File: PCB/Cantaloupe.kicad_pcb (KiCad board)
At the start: 2 copper layers, 149.9 x 122.2 mm, 117 parts, among them J1 RGB_Out, J2 SWD, J3 Trackpad, J4 OLED, J5 Extra, J6 USB_In, J7 Split_comm_link, Q1 AO6802, SW1 MX, SW10 MX, SW11 MX, SW12 MX, SW13 MX, SW14 MX, SW15 MX, SW16 MX, SW17 MX, SW18 MX, SW19 MX, SW2 MX, SW20 MX, SW21 MX, SW22 MX, SW23 MX, SW24 MX, SW25 MX, SW26 MX, SW27 MX, SW28 MX, SW29 MX, SW3 MX, SW30 MX, SW31 Encoder, SW32 Reset, SW4 MX, SW5 MX, SW6 MX, SW7 MX, SW8 MX, SW9 MX, U1 STM32F401CCU6, U2 MB85RS64, U3 SRV05-4, U4 SRV05-4, U5 W25Q128JVS, U6 XC6206P332MR, Y1 8MHz

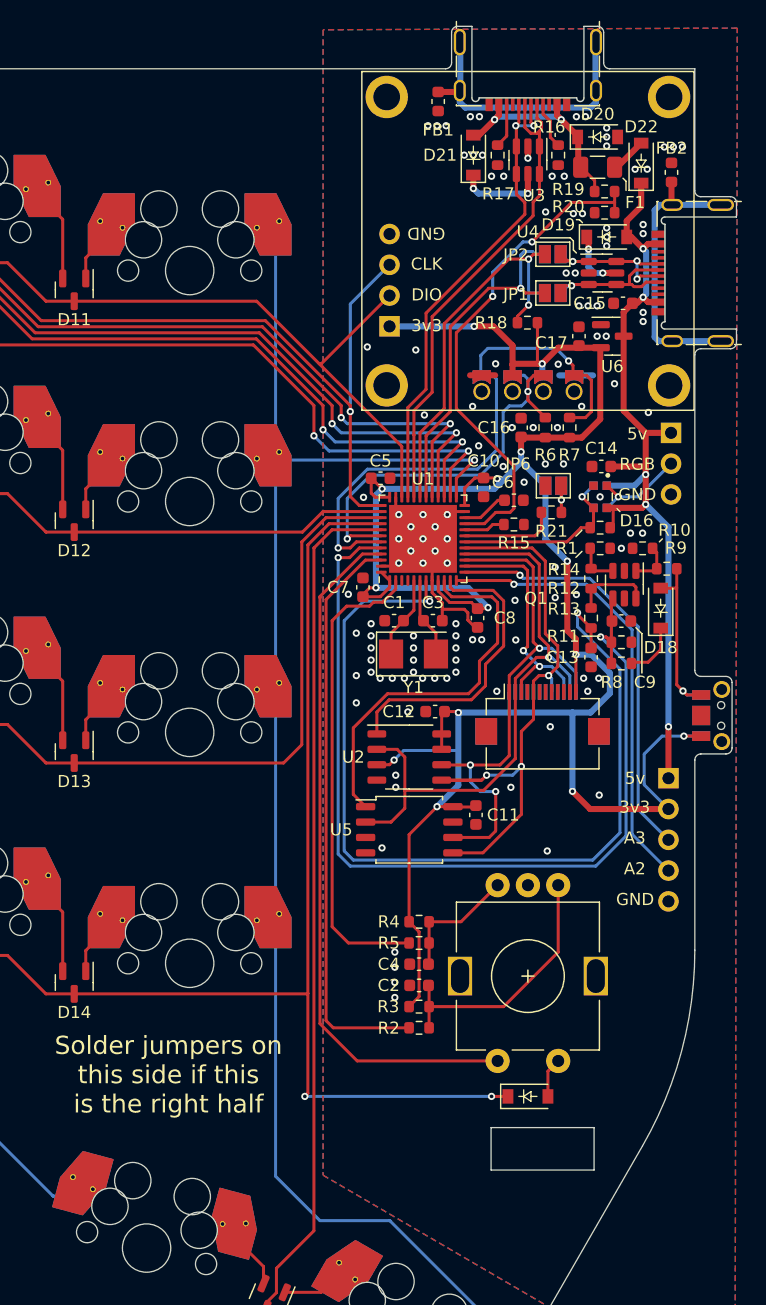
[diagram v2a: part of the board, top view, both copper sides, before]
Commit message: 30/5/2022 changes
Changed XC6206P332MR-G to XC6220B331MR-G for more power output. Changed fuse to 1A. Fixed library links. Changed AO6802 back to two AO3400s. Moved reset circuit downwards and extra pin header upwards for better routing. Updated BOM.
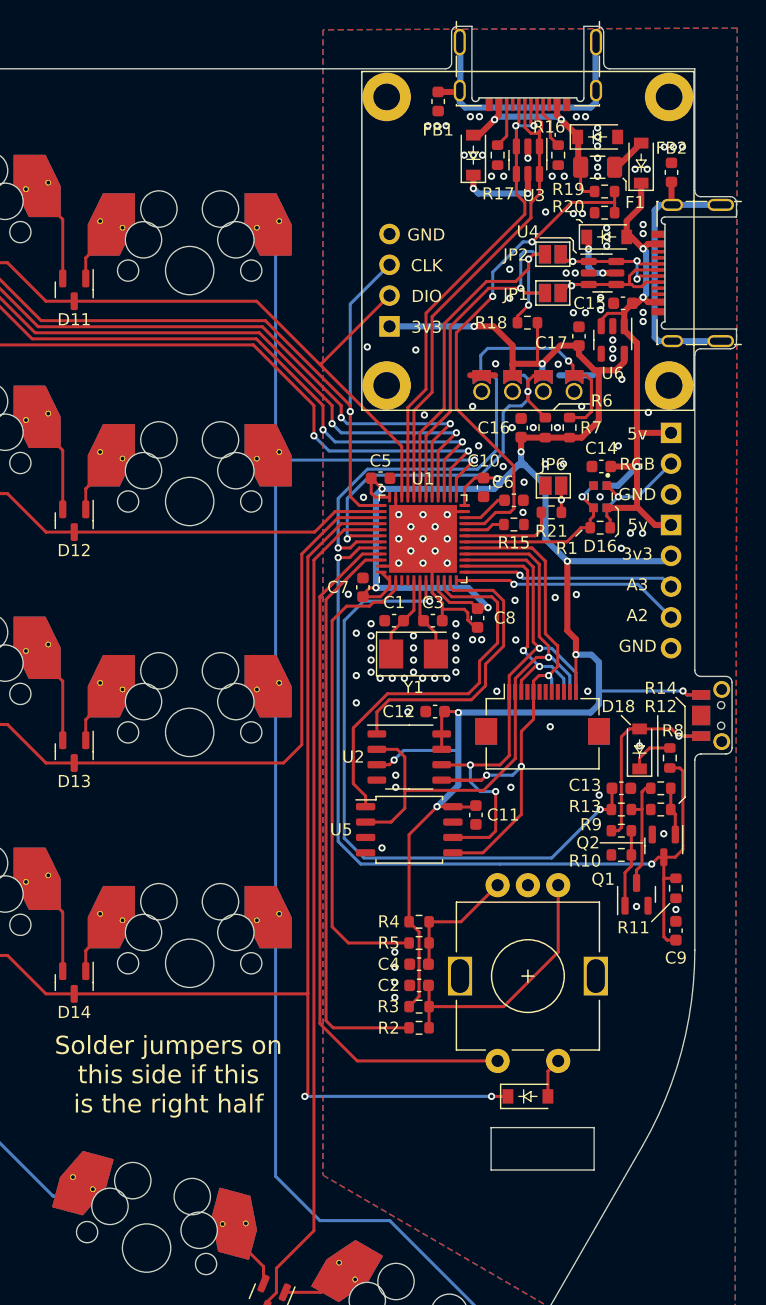
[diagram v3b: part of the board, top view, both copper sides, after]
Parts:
- added Q2: AO3400A, Package_TO_SOT_SMD:SOT-23, F.Cu at (201.3, 116.2)
- A1: footprint Ariamelon:Ariamelon_Logo_x3_CU -> Cantaloupe:Ariamelon_Logo_x3_CU
- D16: footprint Ariamelon:LED_WS2812-2020_Flippable -> Cantaloupe:LED_WS2812-2020_Flippable
- D17, D18, D20: footprint Ariamelon:D_SOD-123 -> Cantaloupe:D_SOD-123
- D19, D21, D22: value B5819W-TP -> B5819W SL; footprint Ariamelon:D_SOD-123 -> Cantaloupe:D_SOD-123
- F1: value nSMD050 -> nSMD100
- J1: footprint Ariamelon:PinHeader_1x03_P2.54mm_Vertical_Silkless -> Cantaloupe:PinHeader_1x03_P2.54mm_Vertical_Silkless
- J2: footprint Ariamelon:PinHeader_1x04_P2.54mm_Vertical_SIlkless -> Cantaloupe:PinHeader_1x04_P2.54mm_Vertical_SIlkless
- J3: footprint Ariamelon:Hirose_FH12-12S-0.5SH_1x12-1MP_P0.50mm_Horizontal_Flippable -> Cantaloupe:Hirose_FH12-12S-0.5SH_1x12-1MP_P0.50mm_Horizontal_Flippable
- J4: footprint Ariamelon:OLED_0.96_SSD1306_128x64_Flippable_Reversepads -> Cantaloupe:OLED_0.96_SSD1306_128x64_Flippable_Reversepads
- J5: footprint Ariamelon:PinHeader_1x05_P2.54mm_Vertical_Silkless -> Cantaloupe:PinHeader_1x05_P2.54mm_Vertical_Silkless
- J6, J7: footprint Ariamelon:HRO-TYPE-C-31-M-13x -> Cantaloupe:HRO-TYPE-C-31-M-13x
- Q1: value AO6802 -> AO3400A; footprint Package_TO_SOT_SMD:SOT-23-6 -> Package_TO_SOT_SMD:SOT-23
- R19: value 100k -> 5.1k
- R20: value 200k -> 10k
- R6, R7: value 4.7k -> 4k7
- SW1, SW10, SW11, SW12, SW13, SW14, SW15, SW16, SW17, SW18, SW19, SW2, SW20, SW21, SW22, SW23, SW24, SW25, SW26, SW27, SW28, SW29, SW3, SW30, SW4, SW5, SW6, SW7, SW8, SW9: footprint Ariamelon:MXOnly-1U-Hotswap-Dual -> Cantaloupe:MXOnly-1U-Hotswap-Dual
- SW31: footprint Ariamelon:EC11_Flippable -> Cantaloupe:EC11_Flippable
- SW32: footprint Ariamelon:Switch_TS24ZJ_Flippable -> Cantaloupe:Switch_TS24ZJ_Flippable
- U6: value XC6206P332MR -> XC6220B331MR-G; footprint Package_TO_SOT_SMD:SOT-23 -> Package_TO_SOT_SMD:SOT-23-5
- moved C9 25.9 mm to (202.3, 123.2), turned to 90 degrees
- moved Q1 25.6 mm to (199.1, 120.2), turned to 90 degrees
- moved R10 25.4 mm to (197.8, 116.9)
- moved R14 22.1 mm to (201.1, 113.2), turned to 180 degrees
- moved R9 21.9 mm to (197.8, 114.9), turned to 0 degrees
- moved J5 20.9 mm to (201.9, 89.7)
- moved R11 20.8 mm to (202.3, 119.7), turned to -90 degrees
- moved R12 18.2 mm to (201.1, 111.4), turned to 180 degrees
- moved R13 16.0 mm to (197.8, 113.2), turned to 180 degrees
- moved D18 11.7 mm to (199.3, 108.2)
- moved C13 11.1 mm to (197.8, 111.4), turned to 180 degrees
- moved R8 8.77 mm to (201.8, 108.9), turned to 90 degrees
- moved U6 0.32 mm to (197.1, 74.5), turned to -90 degrees
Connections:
- Q1 pad 3: Net-(Q1-Pad3) -> Net-(R12-Pad2)
- R12 pad 1: Net-(Q1-Pad3) -> Net-(R12-Pad1)
- R12 pad 2: Net-(Q1-Pad6) -> Net-(R12-Pad2)
- R13 pad 1: Net-(Q1-Pad6) -> Net-(R12-Pad2)
- R14 pad 1: Net-(Q1-Pad3) -> Net-(R12-Pad1)
- SW32 pad 1: Net-(D18-Pad2) -> +3V3
- SW32 pad 2: +3V3 -> Net-(D18-Pad2)
- U6 pad 1: GND -> +5V
- U6 pad 2: +3V3 -> GND
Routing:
- net NRST: track 75.5 -> 53.6 mm
- net +5V: track 69.8 -> 50.7 mm, vias 5 -> 3
- net A2: track 37.3 -> 19.0 mm
- net A3: track 34.8 -> 17.5 mm
- net Net-(R12-Pad2): track 0.00 -> 9.44 mm
- net Net-(Q1-Pad6): track 6.45 -> 0.00 mm
- net +3V3: track 200.7 -> 194.8 mm, vias 14 -> 13
- net Net-(R12-Pad1): track 0.00 -> 3.97 mm
- net BOOT0: track 77.1 -> 73.4 mm
- net Net-(Q1-Pad3): track 3.21 -> 0.00 mm
- net Net-(D18-Pad2): track 14.9 -> 18.0 mm
- net Net-(R10-Pad2): track 3.37 -> 6.40 mm
- net Link-: track 12.1 -> 13.0 mm
- net Net-(D18-Pad1): track 4.52 -> 3.74 mm
- net ROW3: track 168.9 -> 168.3 mm
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
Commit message: Better routing
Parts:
- FB1, FB2: value BLM18KG260 -> GZ1608D110TF
- SW1, SW10, SW11, SW12, SW13, SW14, SW15, SW16, SW17, SW18, SW19, SW2, SW20, SW21, SW22, SW23, SW24, SW25, SW26, SW27, SW28, SW29, SW3, SW30, SW4, SW5, SW6, SW7, SW8, SW9: footprint Cantaloupe:MXOnly-1U-Hotswap-Dual -> Cantaloupe:MX_Choc-1U-Hotswap-Dual
- U1: value STM32F401CCU6 -> STM32F411CCU6
- moved D1 5.50 mm to (79.0, 79.2)
- moved D2 5.50 mm to (79.0, 98.2)
- moved D4 5.50 mm to (79.0, 136.3)
- moved D5 5.50 mm to (79.0, 155.4)
- moved D3 5.50 mm to (79.0, 117.3)
- moved D11 3.91 mm to (152.7, 74.2)
- moved D12 3.91 mm to (152.7, 93.3)
- moved D14 3.91 mm to (152.7, 131.4)
- moved D13 3.91 mm to (152.7, 112.3)
- moved D6 3.65 mm to (117.2, 69.7)
- moved D7 3.65 mm to (117.2, 88.7)
- moved D8 3.65 mm to (117.2, 107.8)
- moved D10 3.65 mm to (117.2, 145.9)
- moved D9 3.65 mm to (117.2, 126.8)
- moved A1 1.59 mm to (128.7, 131.9)
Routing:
- net COL0: track 231.8 -> 308.9 mm
- net COL2: track 183.3 -> 257.7 mm
- net COL5: track 119.9 -> 181.7 mm
- net COL4: track 154.5 -> 215.5 mm
- net COL1: track 193.7 -> 248.1 mm
- net COL3: track 158.0 -> 210.3 mm
- net Net-(D2-Pad2): track 3.81 -> 23.0 mm
- net Net-(D1-Pad2): track 3.81 -> 23.0 mm
- net Net-(D3-Pad2): track 3.81 -> 23.0 mm
- net Net-(D4-Pad2): track 3.81 -> 23.0 mm
- net Net-(D5-Pad2): track 3.81 -> 23.0 mm
- net Net-(D9-Pad2): track 3.81 -> 22.1 mm
- net Net-(D6-Pad2): track 3.81 -> 22.1 mm
- net Net-(D8-Pad2): track 3.81 -> 22.1 mm
- net Net-(D7-Pad2): track 3.81 -> 22.1 mm
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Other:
- board text added: "Cantaloupe V2.2"
- board text removed: "Cantaloupe V2.1"

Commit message: INCOMPLETE V3.0 Initial Update
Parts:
- removed J7: Split_comm_link, Cantaloupe:HRO-TYPE-C-31-M-13x
- removed JP4: Link+_L, Jumper:SolderJumper-2_P1.3mm_Open_Pad1.0x1.5mm
- removed JP5: Side_L, Jumper:SolderJumper-2_P1.3mm_Open_Pad1.0x1.5mm
- removed JP6: Side_R, Jumper:SolderJumper-2_P1.3mm_Open_Pad1.0x1.5mm
- removed Q2: AO3400A, Package_TO_SOT_SMD:SOT-23
- removed R21: 10k, Resistor_SMD:R_0603_1608Metric
- added C18: 100n, Capacitor_SMD:C_0402_1005Metric, B.Cu at (138.6, 57.1)
- added C19: 4u7, Capacitor_SMD:C_0603_1608Metric, B.Cu at (153.7, 103.9)
- added C20: 100n, Capacitor_SMD:C_0402_1005Metric, B.Cu at (153.7, 106.4)
- added C21: 100n, Capacitor_SMD:C_0402_1005Metric, B.Cu at (144.6, 46.2)
- added C22: 100n, Capacitor_SMD:C_0402_1005Metric, B.Cu at (147.4, 50.5)
- added C23: 100n, Capacitor_SMD:C_0402_1005Metric, B.Cu at (132.7, 50.5)
- added C24: 1u, Capacitor_SMD:C_0603_1608Metric, B.Cu at (153.8, 90.0)
- added C25: 100n, Cantaloupe:C_0402_1005Metric, B.Cu at (16.6, 55.4)
- added C26: 100n, Cantaloupe:C_0402_1005Metric, B.Cu at (26.2, 75.9)
- added C27: 100n, Cantaloupe:C_0402_1005Metric, B.Cu at (16.6, 93.5)
- added C28: 100n, Cantaloupe:C_0402_1005Metric, B.Cu at (26.2, 114.0)
- added C29: 100n, Cantaloupe:C_0402_1005Metric, B.Cu at (16.6, 131.6)
- added C30: 100n, Cantaloupe:C_0402_1005Metric, B.Cu at (35.6, 53.0)
- added C31: 100n, Cantaloupe:C_0402_1005Metric, B.Cu at (45.2, 73.5)
- added C32: 100n, Cantaloupe:C_0402_1005Metric, B.Cu at (35.6, 91.1)
- added C33: 100n, Cantaloupe:C_0402_1005Metric, B.Cu at (45.2, 111.6)
- added C34: 100n, Cantaloupe:C_0402_1005Metric, B.Cu at (35.6, 129.2)
- added C35: 100n, Cantaloupe:C_0402_1005Metric, B.Cu at (54.7, 48.3)
- added C36: 100n, Cantaloupe:C_0402_1005Metric, B.Cu at (64.3, 68.8)
- added C37: 100n, Cantaloupe:C_0402_1005Metric, B.Cu at (54.7, 86.4)
- added C38: 100n, Cantaloupe:C_0402_1005Metric, B.Cu at (64.3, 106.9)
- added C39: 100n, Cantaloupe:C_0402_1005Metric, B.Cu at (54.7, 124.5)
- added C40: 100n, Cantaloupe:C_0402_1005Metric, B.Cu at (73.7, 44.3)
- added C41: 100n, Cantaloupe:C_0402_1005Metric, B.Cu at (83.3, 64.8)
- added C42: 100n, Cantaloupe:C_0402_1005Metric, B.Cu at (73.7, 82.4)
- added C43: 100n, Cantaloupe:C_0402_1005Metric, B.Cu at (83.3, 102.9)
- added C44: 100n, Cantaloupe:C_0402_1005Metric, B.Cu at (86.4, 129.2)
- added C45: 100n, Cantaloupe:C_0402_1005Metric, B.Cu at (92.8, 48.3)
- added C46: 100n, Cantaloupe:C_0402_1005Metric, B.Cu at (102.4, 68.8)
- added C47: 100n, Cantaloupe:C_0402_1005Metric, B.Cu at (92.8, 86.4)
- added C48: 100n, Cantaloupe:C_0402_1005Metric, B.Cu at (102.4, 106.9)
- added C49: 100n, Cantaloupe:C_0402_1005Metric, B.Cu at (107.4, 130.7)
- added C50: 100n, Cantaloupe:C_0402_1005Metric, B.Cu at (111.8, 51.5)
- added C51: 100n, Cantaloupe:C_0402_1005Metric, B.Cu at (121.4, 72.0)
- added C52: 100n, Cantaloupe:C_0402_1005Metric, B.Cu at (111.8, 89.6)
- added C53: 100n, Cantaloupe:C_0402_1005Metric, B.Cu at (121.4, 110.1)
- added C54: 100n, Cantaloupe:C_0402_1005Metric, B.Cu at (127.1, 137.6)
- added D23: 1N4148, Cantaloupe:D_SOD-323, B.Cu at (88.4, 75.6)
- added D24: 1N4148, Cantaloupe:D_SOD-323, B.Cu at (88.4, 94.6)
- added D25: 1N4148, Cantaloupe:D_SOD-323, B.Cu at (105.9, 119.1)
- added D26: 1N4148, Cantaloupe:D_SOD-323, B.Cu at (107.4, 40.7)
- added D27: 1N4148, Cantaloupe:D_SOD-323, B.Cu at (107.4, 59.7)
- added D28: 1N4148, Cantaloupe:D_SOD-323, B.Cu at (107.4, 78.8)
- added D29: 1N4148, Cantaloupe:D_SOD-323, B.Cu at (107.4, 97.8)
- added D30: 1N4148, Cantaloupe:D_SOD-323, B.Cu at (128.7, 126.0)
- added D31: SK6812MINI-E, Cantaloupe:YS-SK6812MINI-E-Flippable, B.Cu at (21.4, 56.1)
- added D32: SK6812MINI-E, Cantaloupe:YS-SK6812MINI-E-Flippable, B.Cu at (21.4, 75.2)
- added D33: SK6812MINI-E, Cantaloupe:YS-SK6812MINI-E-Flippable, B.Cu at (21.4, 94.2)
- added D34: SK6812MINI-E, Cantaloupe:YS-SK6812MINI-E-Flippable, B.Cu at (21.4, 113.3)
- added D35: SK6812MINI-E, Cantaloupe:YS-SK6812MINI-E-Flippable, B.Cu at (21.4, 132.3)
- added D36: SK6812MINI-E, Cantaloupe:YS-SK6812MINI-E-Flippable, B.Cu at (40.4, 53.8)
- added D37: SK6812MINI-E, Cantaloupe:YS-SK6812MINI-E-Flippable, B.Cu at (40.4, 72.8)
- added D38: SK6812MINI-E, Cantaloupe:YS-SK6812MINI-E-Flippable, B.Cu at (40.4, 91.9)
- added D39: SK6812MINI-E, Cantaloupe:YS-SK6812MINI-E-Flippable, B.Cu at (40.4, 110.9)
- added D40: SK6812MINI-E, Cantaloupe:YS-SK6812MINI-E-Flippable, B.Cu at (40.4, 130.0)
- added D41: SK6812MINI-E, Cantaloupe:YS-SK6812MINI-E-Flippable, B.Cu at (59.5, 49.0)
- added D42: SK6812MINI-E, Cantaloupe:YS-SK6812MINI-E-Flippable, B.Cu at (59.5, 68.1)
- added D43: SK6812MINI-E, Cantaloupe:YS-SK6812MINI-E-Flippable, B.Cu at (59.5, 87.1)
- added D44: SK6812MINI-E, Cantaloupe:YS-SK6812MINI-E-Flippable, B.Cu at (59.5, 106.2)
- added D45: SK6812MINI-E, Cantaloupe:YS-SK6812MINI-E-Flippable, B.Cu at (59.5, 125.2)
- added D46: SK6812MINI-E, Cantaloupe:YS-SK6812MINI-E-Flippable, B.Cu at (78.5, 45.0)
- added D47: SK6812MINI-E, Cantaloupe:YS-SK6812MINI-E-Flippable, B.Cu at (78.5, 64.1)
- added D48: SK6812MINI-E, Cantaloupe:YS-SK6812MINI-E-Flippable, B.Cu at (78.5, 83.1)
- added D49: SK6812MINI-E, Cantaloupe:YS-SK6812MINI-E-Flippable, B.Cu at (78.5, 102.2)
- added D50: SK6812MINI-E, Cantaloupe:YS-SK6812MINI-E-Flippable, B.Cu at (91.2, 130.0)
- added D51: SK6812MINI-E, Cantaloupe:YS-SK6812MINI-E-Flippable, B.Cu at (97.6, 49.0)
- added D52: SK6812MINI-E, Cantaloupe:YS-SK6812MINI-E-Flippable, B.Cu at (97.6, 68.1)
- added D53: SK6812MINI-E, Cantaloupe:YS-SK6812MINI-E-Flippable, B.Cu at (97.6, 87.1)
- added D54: SK6812MINI-E, Cantaloupe:YS-SK6812MINI-E-Flippable, B.Cu at (97.6, 106.2)
- added D55: SK6812MINI-E, Cantaloupe:YS-SK6812MINI-E-Flippable, B.Cu at (111.8, 132.7)
- added D56: SK6812MINI-E, Cantaloupe:YS-SK6812MINI-E-Flippable, B.Cu at (116.6, 52.2)
- added D57: SK6812MINI-E, Cantaloupe:YS-SK6812MINI-E-Flippable, B.Cu at (116.6, 71.2)
- added D58: SK6812MINI-E, Cantaloupe:YS-SK6812MINI-E-Flippable, B.Cu at (116.6, 90.3)
- added D59: SK6812MINI-E, Cantaloupe:YS-SK6812MINI-E-Flippable, B.Cu at (116.6, 109.3)
- added D60: SK6812MINI-E, Cantaloupe:YS-SK6812MINI-E-Flippable, B.Cu at (130.9, 140.6)
- added D67: B5819W SL, Cantaloupe:D_SOD-123, B.Cu at (141.3, 35.7)
- added D68: SMF5.0A, Cantaloupe:D_SOD-123, B.Cu at (116.1, 34.6)
- added D69: B5819W SL, Cantaloupe:D_SOD-123, B.Cu at (116.1, 37.1)
- added D70: B5819W SL, Cantaloupe:D_SOD-123, B.Cu at (125.7, 37.1)
- added H1: Tooling Hole, Cantaloupe:JLC Tooling Hole, F.Cu at (156.8, 30.3)
- added H2: Tooling Hole, Cantaloupe:JLC Tooling Hole, F.Cu at (11.2, 41.7)
- added H3: Tooling Hole, Cantaloupe:JLC Tooling Hole, F.Cu at (137.0, 150.1)
- added SW33: Reset, Cantaloupe:SW_SPST_TL3342-Dual, F.Cu at (154.7, 63.3)
- added U7: AP2127K-ADJ, Package_TO_SOT_SMD:SOT-23-5, B.Cu at (155.3, 86.3)
- A1, F1, Q1, U4: moved to B.Cu
- C1: value 20p -> 10n; footprint Capacitor_SMD:C_0603_1608Metric -> Capacitor_SMD:C_0402_1005Metric; moved to B.Cu
- C10, C13, C14: footprint Capacitor_SMD:C_0603_1608Metric -> Capacitor_SMD:C_0402_1005Metric; moved to B.Cu
- C11, C12, C5: value 100n -> 1u; moved to B.Cu
- C15, C16, C17, C9: value 10u -> 100n; footprint Capacitor_SMD:C_0603_1608Metric -> Capacitor_SMD:C_0402_1005Metric; moved to B.Cu
- C2: value 100n -> 10n; footprint Capacitor_SMD:C_0603_1608Metric -> Capacitor_SMD:C_0402_1005Metric; moved to B.Cu
- C3: value 20p -> 4u7; moved to B.Cu
- C4: value 100n -> 4u7; moved to B.Cu
- C6: value 4.7u -> 100n; footprint Capacitor_SMD:C_0603_1608Metric -> Capacitor_SMD:C_0402_1005Metric; moved to B.Cu
- C7, C8: value 100n -> 22p; footprint Capacitor_SMD:C_0603_1608Metric -> Capacitor_SMD:C_0402_1005Metric; moved to B.Cu
- D1, D10, D11, D12, D13, D14, D15, D2, D3, D4, D5, D6, D7, D8, D9: value D_Dual_CommonCathode_AAK_Split_Small -> 1N4148; footprint Package_TO_SOT_SMD:SOT-23 -> Cantaloupe:D_SOD-323; moved to B.Cu
- D16: value WS2812C-2020 -> 1N4148; footprint Cantaloupe:LED_WS2812-2020_Flippable -> Cantaloupe:D_SOD-323; moved to B.Cu
- D17, D18: value D -> 1N4148; footprint Cantaloupe:D_SOD-123 -> Cantaloupe:D_SOD-323; moved to B.Cu
- D19, D21, D22: value B5819W SL -> 1N4148; footprint Cantaloupe:D_SOD-123 -> Cantaloupe:D_SOD-323; moved to B.Cu
- D20: value SMF5.0A -> 1N4148; footprint Cantaloupe:D_SOD-123 -> Cantaloupe:D_SOD-323; moved to B.Cu
- FB1, FB2: value GZ1608D110TF -> 60R@100MHz; footprint Inductor_SMD:L_0603_1608Metric -> Inductor_SMD:L_1206_3216Metric; moved to B.Cu
- J1: value RGB_Out -> SWD; footprint Cantaloupe:PinHeader_1x03_P2.54mm_Vertical_Silkless -> Connector_PinHeader_2.54mm:PinHeader_1x04_P2.54mm_Vertical
- J2: value SWD -> USB_In; footprint Cantaloupe:PinHeader_1x04_P2.54mm_Vertical_SIlkless -> Cantaloupe:HRO-TYPE-C-31-M-13x
- J3: value Trackpad -> Split_comm_link; footprint Cantaloupe:Hirose_FH12-12S-0.5SH_1x12-1MP_P0.50mm_Horizontal_Flippable -> Cantaloupe:HRO-TYPE-C-31-M-13x; moved to B.Cu
- J4: value OLED -> Trackpad; footprint Cantaloupe:OLED_0.96_SSD1306_128x64_Flippable_Reversepads -> Cantaloupe:Hirose_FH12-12S-0.5SH_1x12-1MP_P0.50mm_Horizontal_Flippable; moved to B.Cu
- J5: value Extra -> OLED; footprint Cantaloupe:PinHeader_1x05_P2.54mm_Vertical_Silkless -> Cantaloupe:OLED_1.5_SSD1315_128x128_NoPins
- J6: value USB_In -> OLED_PH; footprint Cantaloupe:HRO-TYPE-C-31-M-13x -> Cantaloupe:JST_PH_S7B-PH-K_1x07_P2.00mm_Horizontal-Dual
- JP1: value Link-_R -> Side_L; moved to B.Cu
- JP2: value Link+_R -> Side_R; moved to B.Cu
- JP3: value Link-_L -> MISO_Pullup
- R1, R16, R17: value 5k1 -> 10k; footprint Resistor_SMD:R_0603_1608Metric -> Resistor_SMD:R_0402_1005Metric; moved to B.Cu
- R10: value 10k -> 1k; footprint Resistor_SMD:R_0603_1608Metric -> Resistor_SMD:R_0402_1005Metric; moved to B.Cu
- R11: value 1M -> 5k1; footprint Resistor_SMD:R_0603_1608Metric -> Resistor_SMD:R_0402_1005Metric; moved to B.Cu
- R12: value 10k -> 5k1; footprint Resistor_SMD:R_0603_1608Metric -> Resistor_SMD:R_0402_1005Metric; moved to B.Cu
- R13: value 100 -> 10k; footprint Resistor_SMD:R_0603_1608Metric -> Resistor_SMD:R_0402_1005Metric; moved to B.Cu
- R14: value 100k -> 39; footprint Resistor_SMD:R_0603_1608Metric -> Resistor_SMD:R_0402_1005Metric; moved to B.Cu
- R15: value 100k -> 10k; footprint Resistor_SMD:R_0603_1608Metric -> Resistor_SMD:R_0402_1005Metric; moved to B.Cu
- R18: value 10k -> 15k; footprint Resistor_SMD:R_0603_1608Metric -> Resistor_SMD:R_0402_1005Metric; moved to B.Cu
- R19: value 5.1k -> 10k; footprint Resistor_SMD:R_0603_1608Metric -> Resistor_SMD:R_0402_1005Metric; moved to B.Cu
- R2, R20, R3, R4, R5: footprint Resistor_SMD:R_0603_1608Metric -> Resistor_SMD:R_0402_1005Metric; moved to B.Cu
- R6, R7: value 4k7 -> 1k; footprint Resistor_SMD:R_0603_1608Metric -> Resistor_SMD:R_0402_1005Metric; moved to B.Cu
- R8: value 100k -> 27; footprint Resistor_SMD:R_0603_1608Metric -> Resistor_SMD:R_0402_1005Metric; moved to B.Cu
- R9: value 1k -> 27; footprint Resistor_SMD:R_0603_1608Metric -> Resistor_SMD:R_0402_1005Metric; moved to B.Cu
- SW1, SW10, SW11, SW12, SW13, SW14, SW15, SW16, SW17, SW18, SW19, SW2, SW20, SW21, SW22, SW23, SW24, SW25, SW26, SW27, SW28, SW29, SW3, SW30, SW4, SW5, SW6, SW7, SW8, SW9: value MX -> CPG151101S11; footprint Cantaloupe:MX_Choc-1U-Hotswap-Dual -> Cantaloupe:MX_1U-Hotswap-Dual; moved to B.Cu
- SW32: value Reset -> USB Boot; footprint Cantaloupe:Switch_TS24ZJ_Flippable -> Cantaloupe:SW_DIP_SPSTx01_Slide_6.7x4.1mm_W8.61mm_P2.54mm_LowProfile-Dual; moved to B.Cu
- U1: value STM32F411CCU6 -> AP2127K-3.3; footprint Package_DFN_QFN:QFN-48-1EP_7x7mm_P0.5mm_EP5.6x5.6mm -> Package_TO_SOT_SMD:SOT-23-5; moved to B.Cu
- U2: value MB85RS64 -> W25Q128JVS; footprint Package_SO:SSOP-8_3.9x5.05mm_P1.27mm -> Package_SO:SOIC-8_5.23x5.23mm_P1.27mm; moved to B.Cu
- U3: value SRV05-4 -> RP2040; footprint Package_TO_SOT_SMD:SOT-23-6 -> Cantaloupe:QFN-56-1EP_7x7mm_P0.4mm_EP3.2x3.2mm_ThermalVias; moved to B.Cu
- U5: value W25Q128JVS -> SRV05-4; footprint Package_SO:SOIC-8_5.275x5.275mm_P1.27mm -> Package_TO_SOT_SMD:SOT-23-6; moved to B.Cu
- U6: value XC6220B331MR-G -> PMW3360DM-T2QU; footprint Package_TO_SOT_SMD:SOT-23-5 -> Cantaloupe:IC_PMW3360DM-T2QU; moved to B.Cu
- Y1: value 8MHz -> 12MHz; footprint Crystal:Crystal_SMD_5032-2Pin_5.0x3.2mm -> Crystal:Crystal_SMD_3225-4Pin_3.2x2.5mm; moved to B.Cu
- moved D17 147.3 mm to (69.3, 52.6), turned to -90 degrees
- moved R1 145.2 mm to (56.8, 131.2), turned to -90 degrees
- moved D16 137.7 mm to (69.3, 33.5)
- moved D18 135.0 mm to (69.3, 71.6), turned to -90 degrees
- moved SW31 130.8 mm to (59.5, 120.5), turned to 0 degrees
- moved D19 129.7 mm to (69.3, 90.7), turned to -90 degrees
- moved D20 129.0 mm to (82.0, 118.4), turned to -90 degrees
- moved C1 125.1 mm to (58.4, 130.7), turned to 180 degrees
- moved D15 125.1 mm to (50.3, 113.7), turned to -90 degrees
- moved R2 122.7 mm to (58.4, 131.8)
- moved R11 122.3 mm to (116.2, 32.8), turned to 0 degrees
- moved C2 120.6 mm to (60.5, 130.7)
- moved R3 120.6 mm to (60.5, 131.8), turned to 0 degrees
- moved R4 119.3 mm to (62.1, 131.2), turned to 90 degrees
- moved D22 111.1 mm to (88.4, 56.5), turned to -90 degrees
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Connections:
- C1 pad 2: HSE_IN -> Net-(C1-Pad2)
- C10 pad 2: +3V3 -> +1V1
- C11 pad 2: +3V3 -> +1V1
- C13 pad 2: NRST -> +3V3
- C14 pad 2: +5V -> +3V3
- C15 pad 2: +5V -> +3V3
- C3 pad 2: HSE_OUT -> +5V
- C4 pad 2: Net-(C4-Pad2) -> +3V3
- C5 pad 1: GND -> +3V3
- C5 pad 2: +3V3 -> GND
- C6 pad 2: Net-(C6-Pad2) -> +3V3
- C7 pad 2: +3V3 -> Net-(U3-XIN)
- C8 pad 2: +3V3 -> Net-(C8-Pad2)
- C9 pad 1: BOOT0 -> GND
- C9 pad 2: GND -> +1V1
- D1 pad 1: Net-(D1-Pad1) -> /MCU/ROW0
- D1 pad 2: Net-(D1-Pad2) -> Net-(D1-A)
- D10 pad 1: Net-(D10-Pad1) -> /MCU/ROW4
- D10 pad 2: Net-(D10-Pad2) -> Net-(D10-A)
- D11 pad 1: Net-(D11-Pad1) -> /MCU/ROW0
- D11 pad 2: Net-(D11-Pad2) -> Net-(D11-A)
- D12 pad 1: Net-(D12-Pad1) -> /MCU/ROW1
- D12 pad 2: Net-(D12-Pad2) -> Net-(D12-A)
- D13 pad 1: Net-(D13-Pad1) -> /MCU/ROW2
- D13 pad 2: Net-(D13-Pad2) -> Net-(D13-A)
- D14 pad 1: Net-(D14-Pad1) -> /MCU/ROW3
- D14 pad 2: Net-(D14-Pad2) -> Net-(D14-A)
- D15 pad 1: Net-(D15-Pad1) -> /MCU/ROW4
- D15 pad 2: Net-(D15-Pad2) -> Net-(D15-A)
- D16 pad 1: Net-(D16-Pad1) -> /MCU/ROW0
- D16 pad 2: GND -> Net-(D16-A)
- D17 pad 1: ROW3 -> /MCU/ROW1
- D17 pad 2: Net-(D17-Pad2) -> Net-(D17-A)
- D18 pad 1: Net-(D18-Pad1) -> /MCU/ROW2
- D18 pad 2: Net-(D18-Pad2) -> Net-(D18-A)
- D19 pad 1: Net-(D19-Pad1) -> /MCU/ROW3
- D19 pad 2: +5V -> Net-(D19-A)
- D2 pad 1: Net-(D2-Pad1) -> /MCU/ROW1
- D2 pad 2: Net-(D2-Pad2) -> Net-(D2-A)
- D20 pad 1: VBUS -> /MCU/ROW4
- D20 pad 2: GND -> Net-(D20-A)
- D21 pad 1: Net-(D21-Pad1) -> /MCU/ROW0
- D21 pad 2: VBUS -> Net-(D21-A)
- D22 pad 1: +5V -> /MCU/ROW1
- D22 pad 2: Net-(D22-Pad2) -> Net-(D22-A)
- D3 pad 1: Net-(D3-Pad1) -> /MCU/ROW2
- D3 pad 2: Net-(D3-Pad2) -> Net-(D3-A)
- D4 pad 1: Net-(D4-Pad1) -> /MCU/ROW3
- D4 pad 2: Net-(D4-Pad2) -> Net-(D4-A)
- D5 pad 1: Net-(D5-Pad1) -> /MCU/ROW4
- D5 pad 2: Net-(D5-Pad2) -> Net-(D5-A)
- D6 pad 1: Net-(D6-Pad1) -> /MCU/ROW0
- D6 pad 2: Net-(D6-Pad2) -> Net-(D6-A)
- D7 pad 1: Net-(D7-Pad1) -> /MCU/ROW1
- D7 pad 2: Net-(D7-Pad2) -> Net-(D7-A)
- D8 pad 1: Net-(D8-Pad1) -> /MCU/ROW2
- D8 pad 2: Net-(D8-Pad2) -> Net-(D8-A)
- D9 pad 1: Net-(D9-Pad1) -> /MCU/ROW3
- D9 pad 2: Net-(D9-Pad2) -> Net-(D9-A)
- F1 pad 1: Net-(D22-Pad2) -> Net-(D70-A)
- FB1 pad 1: GND -> Net-(J2-SHIELD)
- FB1 pad 2: Net-(FB1-Pad2) -> GND
- FB2 pad 1: GND -> Net-(J3-SHIELD)
- FB2 pad 2: Net-(FB2-Pad2) -> GND
- J1 pad 1: +5V -> Net-(J1-Pin_1)
- J1 pad 2: Net-(D16-Pad1) -> GND
- J1 pad 3: GND -> Net-(J1-Pin_3)
- J4 pad 1: GND -> /Comms/SCK
- J4 pad 2: +3V3 -> /Comms/MISO
- J4 pad 3: SCL -> /Comms/SS_TB
- J4 pad 4: SDA -> unconnected-(J4-Pin_4-Pad4)
- JP1 pad 1: TX -> +3V3
- JP1 pad 2: Link- -> Net-(JP1-B)
- JP2 pad 1: RX -> GND
- JP2 pad 2: Link+ -> Net-(JP1-B)
- JP3 pad 1: RX -> Net-(JP3-A)
- JP3 pad 2: Link- -> /Comms/MISO
- Q1 pad 1: Net-(Q1-Pad1) -> +3V3
- Q1 pad 2: GND -> Net-(Q1-S)
- Q1 pad 3: Net-(Q1-Pad3) -> /MCU/RGB
- R1 pad 1: +5V -> Net-(C1-Pad2)
- R1 pad 2: LED -> /MCU/ROTA
- R10 pad 1: GND -> Net-(JP1-B)
- R10 pad 2: Net-(Q1-Pad1) -> /MCU/Side
- R11 pad 1: BOOT0 -> GND
- R11 pad 2: GND -> Net-(J2-CC1)
- R12 pad 1: Net-(Q2-Pad1) -> GND
- R12 pad 2: Net-(Q1-Pad3) -> Net-(J2-CC2)
- R13 pad 1: Net-(Q1-Pad3) -> /Comms/~{RST}_TB
- R13 pad 2: NRST -> +3V3
- R14 pad 1: Net-(Q2-Pad1) -> Net-(U6-LED_P)
- R14 pad 2: GND -> +2V
- R15 pad 1: BOOT1 -> Net-(JP3-A)
- R15 pad 2: GND -> +3V3
- R16 pad 1: GND -> Net-(U7-ADJ)
- R16 pad 2: Net-(J6-PadA5) -> GND
- R17 pad 1: GND -> Net-(SW33-B)
- R17 pad 2: Net-(J6-PadB5) -> +3V3
- R18 pad 1: +3V3 -> +2V
- R18 pad 2: RX -> Net-(U7-ADJ)
- R19 pad 1: VBUS -> Net-(Q1-S)
- R19 pad 2: PLUGGED -> +3V3
- R2 pad 1: ROT_A -> Net-(C1-Pad2)
- R2 pad 2: Net-(C2-Pad2) -> +3V3
- R20 pad 1: PLUGGED -> /MCU/RGB
- R20 pad 2: GND -> +5V
- R3 pad 1: Net-(C2-Pad2) -> +3V3
- R3 pad 2: +3V3 -> Net-(C2-Pad2)
- R4 pad 1: +3V3 -> /MCU/ROTB
- R4 pad 2: Net-(C4-Pad2) -> Net-(C2-Pad2)
- R5 pad 1: Net-(C4-Pad2) -> Net-(U2-~{CS})
- R5 pad 2: ROT_B -> +3V3
- R6 pad 1: SCL -> Net-(R6-Pad1)
- R6 pad 2: +3V3 -> Net-(U2-~{CS})
- R7 pad 1: SDA -> Net-(C8-Pad2)
- R7 pad 2: +3V3 -> Net-(U3-XOUT)
- R8 pad 1: BOOT0 -> /Comms/D+
- R8 pad 2: Net-(D18-Pad1) -> Net-(U3-USB_DP)
- R9 pad 1: Net-(D18-Pad2) -> /Comms/D-
- R9 pad 2: Net-(Q1-Pad1) -> Net-(U3-USB_DM)
- SW1 pad 1: COL0 -> Net-(D1-A)
- SW1 pad 2: Net-(D1-Pad2) -> /MCU/COL0
- SW10 pad 1: Net-(D5-Pad1) -> Net-(D10-A)
- SW10 pad 2: COL1 -> /MCU/COL1
- SW11 pad 1: COL2 -> Net-(D11-A)
- SW11 pad 2: Net-(D6-Pad2) -> /MCU/COL2
- SW12 pad 1: COL2 -> Net-(D12-A)
- SW12 pad 2: Net-(D7-Pad2) -> /MCU/COL2
- SW13 pad 1: COL2 -> Net-(D13-A)
- SW13 pad 2: Net-(D8-Pad2) -> /MCU/COL2
- SW14 pad 1: COL2 -> Net-(D14-A)
- SW14 pad 2: Net-(D9-Pad2) -> /MCU/COL2
- SW15 pad 1: COL2 -> Net-(D15-A)
- SW15 pad 2: Net-(D10-Pad2) -> /MCU/COL2
- SW16 pad 1: Net-(D6-Pad1) -> Net-(D16-A)
- SW16 pad 2: COL3 -> /MCU/COL3
- SW17 pad 1: Net-(D7-Pad1) -> Net-(D17-A)
- SW17 pad 2: COL3 -> /MCU/COL3
- SW18 pad 1: Net-(D8-Pad1) -> Net-(D18-A)
- SW18 pad 2: COL3 -> /MCU/COL3
- SW19 pad 1: Net-(D9-Pad1) -> Net-(D19-A)
- SW19 pad 2: COL3 -> /MCU/COL3
- SW2 pad 1: COL0 -> Net-(D2-A)
- SW2 pad 2: Net-(D2-Pad2) -> /MCU/COL0
- SW20 pad 1: Net-(D10-Pad1) -> Net-(D20-A)
- SW20 pad 2: COL3 -> /MCU/COL3
- SW21 pad 1: COL4 -> Net-(D21-A)
- SW21 pad 2: Net-(D11-Pad2) -> /MCU/COL4
- SW22 pad 1: COL4 -> Net-(D22-A)
- SW22 pad 2: Net-(D12-Pad2) -> /MCU/COL4
- SW23 pad 1: COL4 -> Net-(D23-A)
- SW23 pad 2: Net-(D13-Pad2) -> /MCU/COL4
- SW24 pad 1: COL4 -> Net-(D24-A)
- SW24 pad 2: Net-(D14-Pad2) -> /MCU/COL4
- SW25 pad 1: COL4 -> Net-(D25-A)
- SW25 pad 2: Net-(D15-Pad2) -> /MCU/COL4
- SW26 pad 1: Net-(D11-Pad1) -> Net-(D26-A)
- SW26 pad 2: COL5 -> /MCU/COL5
- SW27 pad 1: Net-(D12-Pad1) -> Net-(D27-A)
- SW27 pad 2: COL5 -> /MCU/COL5
- SW28 pad 1: Net-(D13-Pad1) -> Net-(D28-A)
- SW28 pad 2: COL5 -> /MCU/COL5
- SW29 pad 1: Net-(D14-Pad1) -> Net-(D29-A)
- SW29 pad 2: COL5 -> /MCU/COL5
- SW3 pad 1: COL0 -> Net-(D3-A)
- SW3 pad 2: Net-(D3-Pad2) -> /MCU/COL0
- SW30 pad 1: Net-(D15-Pad1) -> Net-(D30-A)
- SW30 pad 2: COL5 -> /MCU/COL5
- SW31 pad A: Net-(C2-Pad2) -> Net-(C1-Pad2)
- SW31 pad B: Net-(C4-Pad2) -> Net-(C2-Pad2)
- SW31 pad S1: COLROT -> /MCU/COL2
- SW31 pad S2: Net-(D17-Pad2) -> Net-(D15-A)
- SW32 pad 1: +3V3 -> Net-(R6-Pad1)
- SW32 pad 2: Net-(D18-Pad2) -> GND
- SW4 pad 1: COL0 -> Net-(D4-A)
- SW4 pad 2: Net-(D4-Pad2) -> /MCU/COL0
- SW5 pad 1: COL0 -> Net-(D5-A)
- SW5 pad 2: Net-(D5-Pad2) -> /MCU/COL0
- SW6 pad 1: Net-(D1-Pad1) -> Net-(D6-A)
- SW6 pad 2: COL1 -> /MCU/COL1
- SW7 pad 1: Net-(D2-Pad1) -> Net-(D7-A)
- SW7 pad 2: COL1 -> /MCU/COL1
- SW8 pad 1: Net-(D3-Pad1) -> Net-(D8-A)
- SW8 pad 2: COL1 -> /MCU/COL1
- SW9 pad 1: Net-(D4-Pad1) -> Net-(D9-A)
- SW9 pad 2: COL1 -> /MCU/COL1
- U1 pad 1: +3V3 -> +5V
- U1 pad 2: ROT_B -> GND
- U1 pad 3: unconnected-(U1-Pad3) -> +5V
- U1 pad 5: HSE_IN -> +3V3
- U2 pad 1: SS_EEPROM -> Net-(U2-~{CS})
- U2 pad 2: MISO -> Net-(U2-DO(IO1))
- U2 pad 3: +3V3 -> Net-(U2-IO2)
- U2 pad 5: MOSI -> Net-(U2-DI(IO0))
- U2 pad 6: SCK -> Net-(U2-CLK)
- U2 pad 7: +3V3 -> Net-(U2-IO3)
- U3 pad 1: D- -> +3V3
- U3 pad 2: GND -> /Comms/RX
- U3 pad 3: D+ -> /Comms/TX
- U3 pad 4: D+ -> /Comms/SCK
- U3 pad 5: Net-(D21-Pad1) -> /Comms/MOSI
- U3 pad 6: D- -> /Comms/MISO
- U4 pad 1: Link+ -> /Comms/D+
- U4 pad 3: Link- -> /Comms/D-
- U4 pad 4: Link- -> /Comms/D-
- U4 pad 5: Net-(D19-Pad1) -> Net-(D69-K)
- U4 pad 6: Link+ -> /Comms/D+
- U5 pad 1: SS_Flash -> /Comms/TX
- U5 pad 2: MISO -> GND
- U5 pad 3: unconnected-(U5-Pad3) -> /Comms/RX
- U5 pad 4: GND -> /Comms/RX
- U5 pad 5: MOSI -> Net-(D67-K)
- U5 pad 6: SCK -> /Comms/TX
- U6 pad 1: +5V -> unconnected-(U6-NC-Pad1)
- U6 pad 2: GND -> unconnected-(U6-NC-Pad2)
- U6 pad 3: +5V -> Net-(U6-VDDPIX)
- U6 pad 4: unconnected-(U6-Pad4) -> +2V
- Y1 pad 1: HSE_IN -> Net-(U3-XIN)
- Y1 pad 2: HSE_OUT -> GND
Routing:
- net COL0: track 308.9 -> 0.00 mm, vias 1 -> 0
- net COL2: track 257.7 -> 0.00 mm, vias 2 -> 0
- net COL1: track 248.1 -> 0.00 mm, vias 2 -> 0
- net COL4: track 215.5 -> 0.00 mm, vias 2 -> 0
- net COL3: track 210.3 -> 0.00 mm, vias 2 -> 0
- net /MCU/COL0: track 0.00 -> 203.4 mm, vias 0 -> 1
- net /MCU/ROW4: track 0.00 -> 201.7 mm
- net /MCU/COL1: track 0.00 -> 183.9 mm, vias 0 -> 1
- net COL5: track 181.7 -> 0.00 mm, vias 1 -> 0
- net /MCU/ROW3: track 0.00 -> 172.5 mm
- net ROW4: track 169.6 -> 0.00 mm
- net /MCU/COL2: track 0.00 -> 166.9 mm, vias 0 -> 1
- net ROW3: track 166.4 -> 0.00 mm, vias 2 -> 0
- net /MCU/ROTA: track 0.00 -> 159.6 mm, vias 0 -> 2
- net /MCU/COL3: track 0.00 -> 154.6 mm, vias 0 -> 1
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- added copper zone on B.Cu, net +3V3
- added copper zone on B.Cu, net +5V
- added copper zone on F.Cu, net +5V
- added copper zone on B.Cu, net Net-(D70-A)
- added copper zone on B.Cu, net Net-(J2-SHIELD)
- added copper zone on F.Cu, net Net-(J2-SHIELD)
- added copper zone on B.Cu, net Net-(J3-SHIELD)
- added copper zone on F.Cu, net Net-(J3-SHIELD)
- added copper zone on B.Cu, net VBUS
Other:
- board size 149.9 x 122.2 mm -> 148.5 x 127.3 mm
- board text added: "Cantaloupe V3.0"
- board text added: "OLED"
- board text removed: "3v3"
- board text removed: "5v"
- board text removed: "A2"
- board text removed: "A3"
- board text removed: "CLK"
- board text removed: "Cantaloupe V2.2"
- board text removed: "DIO"
- board text removed: "GND"
- board text removed: "RGB"
- board text removed: "Solder jumpers on this side if this is the left half"
- board text removed: "Solder jumpers on this side if this is the right half"
